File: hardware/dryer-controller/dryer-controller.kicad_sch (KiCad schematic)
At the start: 69 parts, among them K1 SRD-05VDC-SL-C, K2 SRD-05VDC-SL-C, Q1 MMBT2222A, Q2 MMBT2222A, Q3 CJ2310, Q4 CJ2310, Q5 CJ2310, SW1 SW-USB, U1 TSR 1-2450

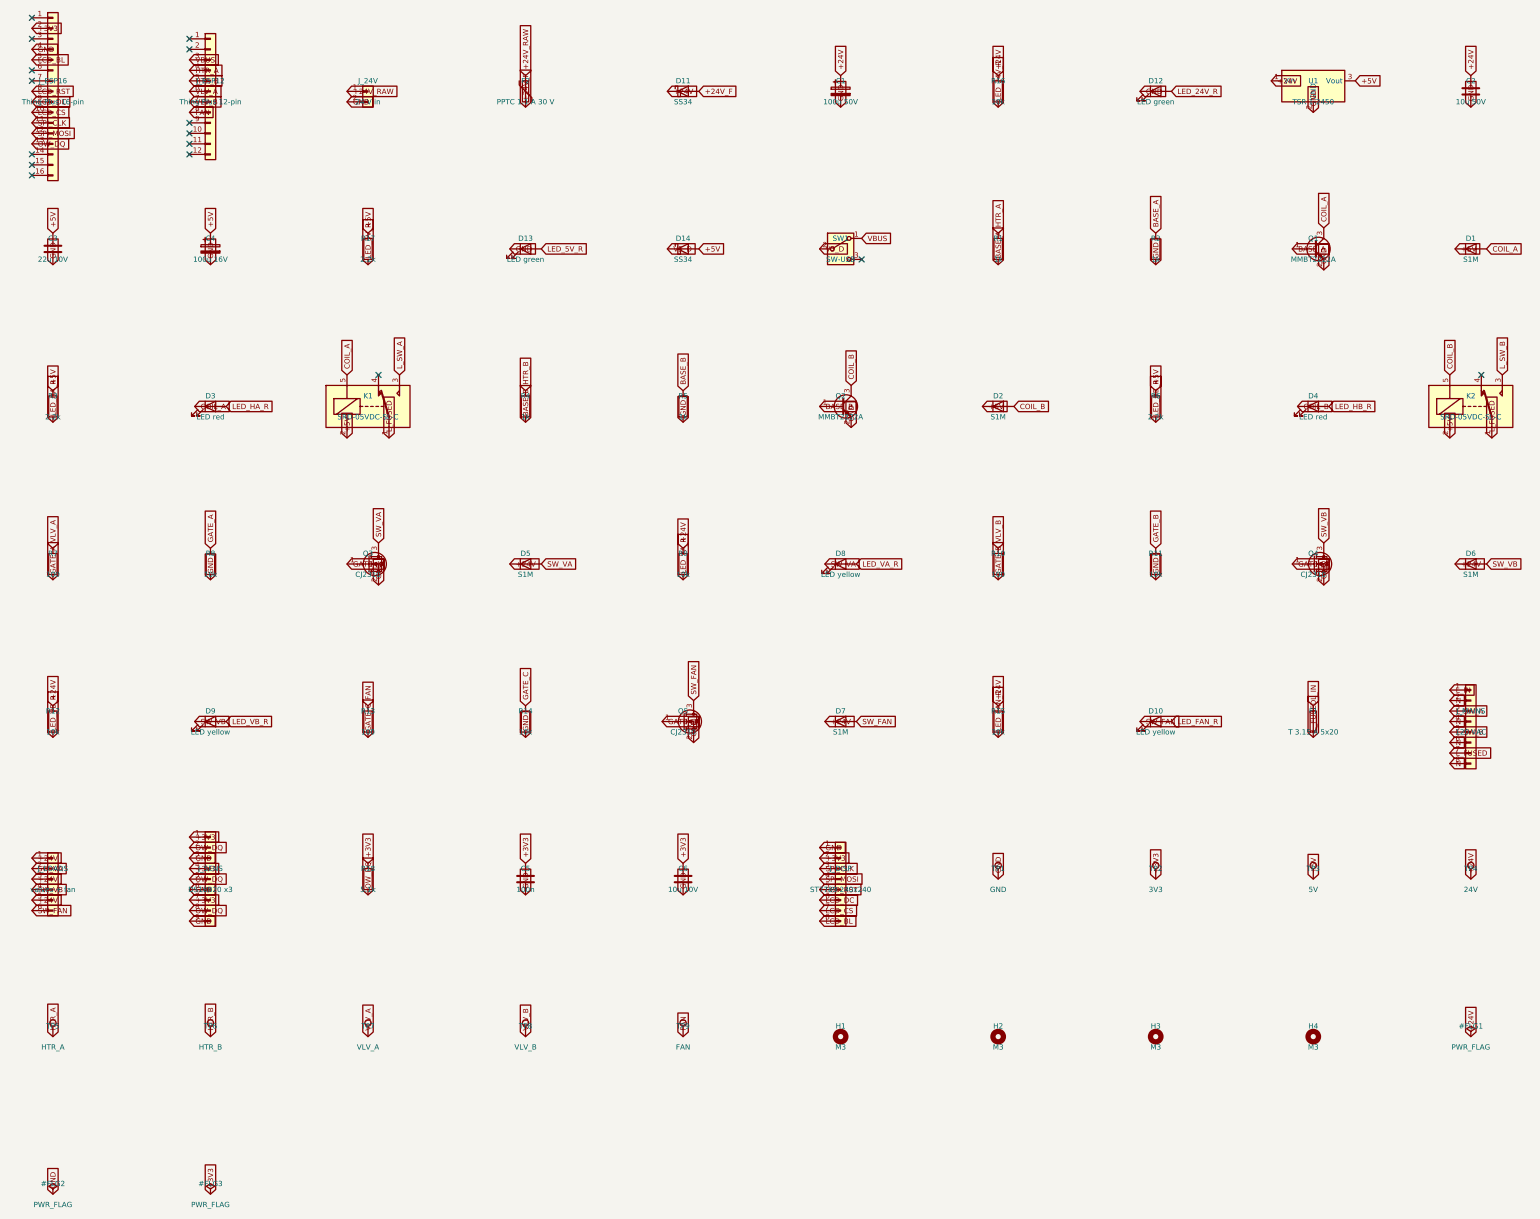
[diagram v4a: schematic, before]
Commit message: Split the design into a controller board and a mains board (review of 2026-10-15)
The single 110 x 85 mm board becomes two: dryer-controller (76 x 85 mm:
the socketed Thing Plus, 24 V in, the 5 V module, SW-USB, the three MOSFET
stages, sensor and display headers, test points) and dryer-mains (64 x 85
mm: F1, both relays with their driver stages, J_MAINS), joined by the
protoboard harness's keyed JST-XH 4-way link (J_RLY / J_CTRL: 5 V, GND,
heater A, heater B). The 1 k base series resistors stay on the controller
and the pulldowns on the mains board, as the protoboard had them. The mains
board is the single board's mains strip moved 48 mm left and 6 mm down on a
2 mm wider board, so the measured clearances hold.

Review items: F1 is a 22.5 mm-pitch footprint with slotted holes (21.5 to
23.5 mm) for the BLX-A style holders on hand, hand-fitted; the PTF-76-B
15 mm footprint stays in the library. U1 is the Amazon-sourced TSR 1-2450,
hand-fitted, with a bench check of its pin order added to the first-article
check. Mounting holes are 4.3 mm (M4) on both boards. The SHT45 stays on
the Thing Plus's Qwiic connector (firmware and pins verified, documented).
PCBWay feasibility is written up in hardware/README.md (advice only).

Generator: circuit.py and placement.py become parts.py (catalogue and
helpers), controller.py and mains.py (each board's parts, nets, geometry,
silk; mains rules and copper in mains.py) and boards.py; every command runs
over both boards unless one is named. The local footprints move to
hardware/lib/dryer.pretty and are copied into each project; the sync check
compares the copies. Outputs and review renders are per board. The board
tests hold one generator-built board at a time: building a second
invalidates the first in pcbnew.

Docs: hardware.md PCB section, board-continuity-check.md PCB section, the
spec's as-built addendum, hardware/README.md, CLAUDE.md, README, releasing,
failure modes, inspection checklist, datasheets (PTF-77, BLX-A, JST XH).

Co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
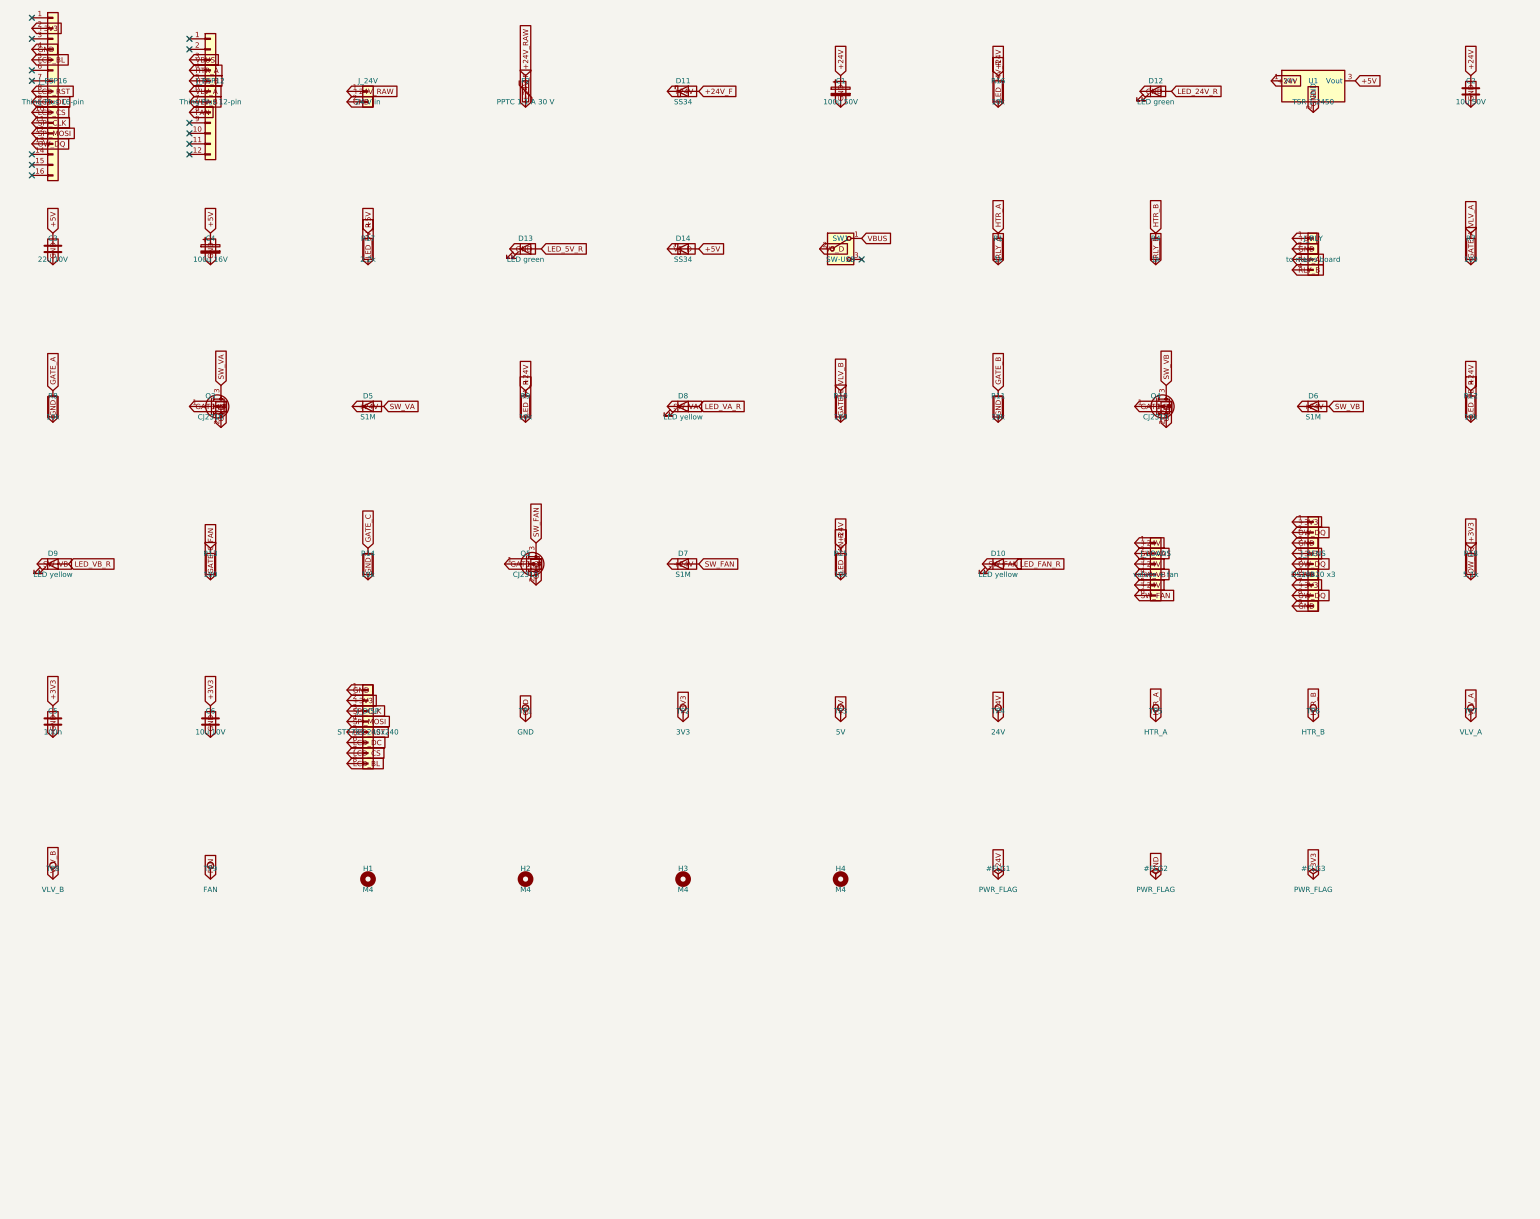
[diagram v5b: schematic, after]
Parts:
- removed D1, D2: S1M, Diode_SMD:D_SMA, symbol Device:D
- removed D3, D4: LED red, LED_SMD:LED_0805_2012Metric, symbol Device:LED
- removed F1: T 3.15 A 5x20, dryer:Fuseholder_5x20mm_Covered_XFCN_PTF-76-B_P15.00mm, symbol Device:Fuse
- removed J_MAINS: 120 VAC, dryer:PhoenixContact_MSTBA_2,5_8-G-5,08_1x08_P5.08mm_Horizontal_Drill1.7mm, symbol Connector_Generic:Conn_01x08
- removed K1, K2: SRD-05VDC-SL-C, Relay_THT:Relay_SPDT_SANYOU_SRD_Series_Form_C, symbol Relay:SANYOU_SRD_Form_C
- removed Q1, Q2: MMBT2222A, Package_TO_SOT_SMD:SOT-23, symbol Transistor_BJT:MMBT2222A
- removed R2, R5: 1k, Resistor_SMD:R_0805_2012Metric, symbol Device:R
- removed R3, R6: 2.2k, Resistor_SMD:R_0805_2012Metric, symbol Device:R
- added J_RLY: to mains board, Connector_JST:JST_XH_B4B-XH-A_1x04_P2.50mm_Vertical, symbol Connector_Generic:Conn_01x04
- H1, H2, H3, H4: value M3 -> M4; footprint MountingHole:MountingHole_3.2mm_M3 -> MountingHole:MountingHole_4.3mm_M4
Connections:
- net +5V: now also J_RLY.1 (Pin_1)
- net GND: now also J_RLY.2 (Pin_2)
- net BASE_A renamed RLY_A
- net RLY_A: now also J_RLY.3 (Pin_3)
- net BASE_B renamed RLY_B
- net RLY_B: now also J_RLY.4 (Pin_4)
- no-connect marks 16 -> 14
